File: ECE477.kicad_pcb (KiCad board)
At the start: 2 copper layers, 88.9 x 88.9 mm, 52 parts, among them IC1 LP3852EMP-3.3_NOPB, IC2 BQ29330DBT, J1 P7805-2000-S, J2 Conn_01x05_Male, J3 Conn_01x05_Male, J4 Conn_01x05_Male, J5 Conn_01x05_Male, J6 Conn_01x05_Male, J7 Conn_01x05_Male, J8 Conn_01x05_Male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

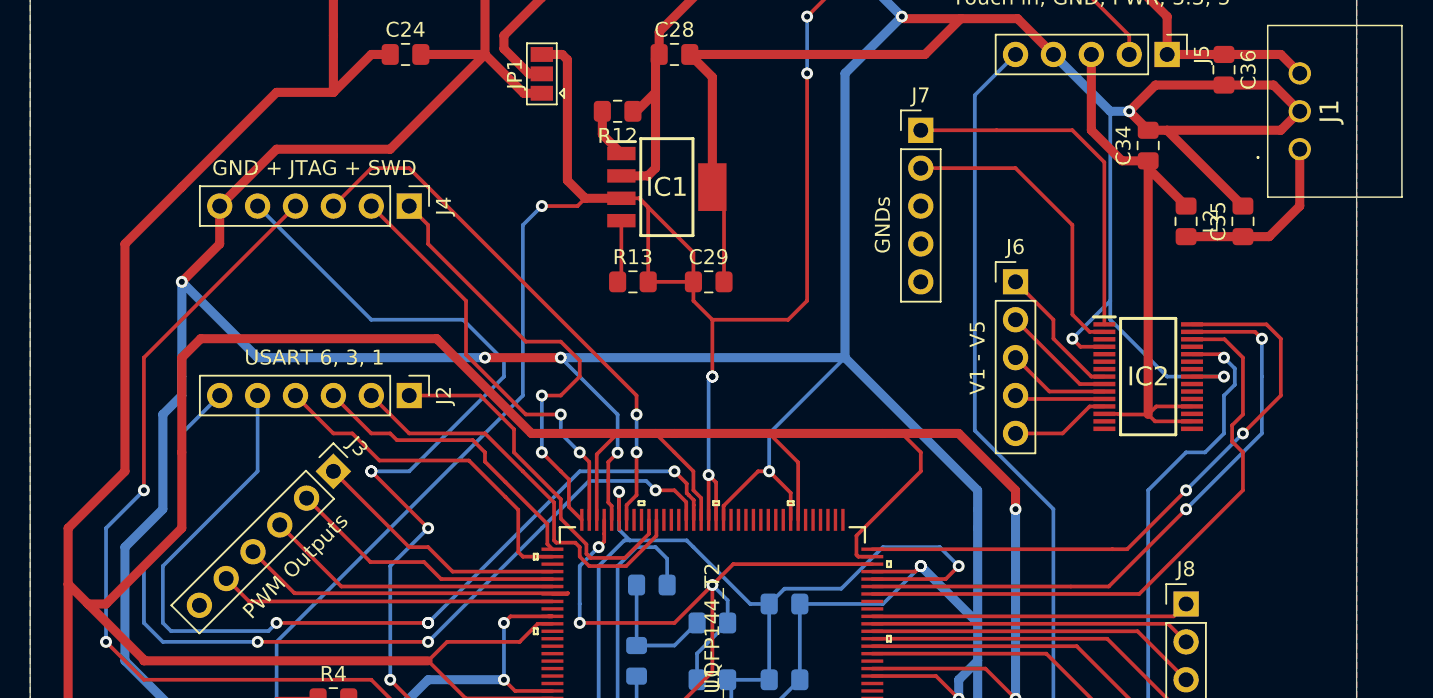
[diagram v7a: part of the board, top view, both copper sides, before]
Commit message: Updated USART GND
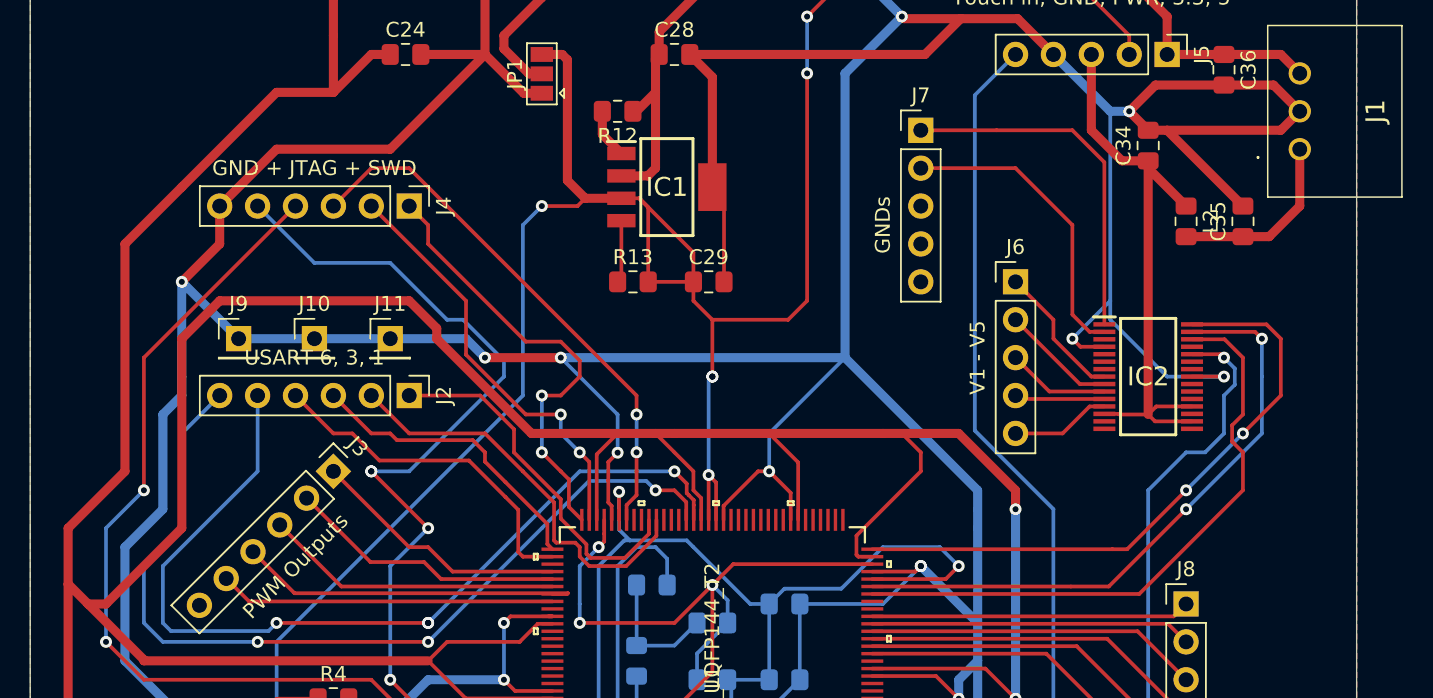
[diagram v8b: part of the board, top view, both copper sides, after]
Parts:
- added J10: Conn_01x01_Male, Connector_PinHeader_2.54mm:PinHeader_1x01_P2.54mm_Vertical, F.Cu at (171.4, 83.8)
- added J11: Conn_01x01_Male, Connector_PinHeader_2.54mm:PinHeader_1x01_P2.54mm_Vertical, F.Cu at (176.5, 83.8)
- added J9: Conn_01x01_Male, Connector_PinHeader_2.54mm:PinHeader_1x01_P2.54mm_Vertical, F.Cu at (166.4, 83.8)
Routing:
- net VDD_MCU: track 485.8 -> 489.0 mm
